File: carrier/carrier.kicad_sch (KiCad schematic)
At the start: 0 parts

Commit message: getting there!!
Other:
- sheet Battery ports: added none; removed +3.3v
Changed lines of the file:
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@@
-    (stroke (width 0) (type solid) (color 0 0 0 0))
-  )
-  (wire (pts (xy 102.235 142.875) (xy 107.95 142.875))
     (stroke (width 0) (type solid) (color 0 0 0 0))
   )
@@
     (effects (font (size 1.27 1.27)) (justify left bottom))
   )
-  (label "+3.3v" (at 102.235 142.875 0)
-    (effects (font (size 1.27 1.27)) (justify left bottom))
-  )
   (label "+1.8v" (at 159.385 50.8 180)
     (effects (font (size 1.27 1.27)) (justify right bottom))
@@
     (pin "BATT" bidirectional (at 146.05 116.205 0)
       (effects (font (size 1.27 1.27)) (justify right))
-    )
-    (pin "+3.3v" input (at 107.95 142.875 180)
-      (effects (font (size 1.27 1.27)) (justify left))
     )
   )
@@
       (reference "#PWR032") (unit 1) (value "GND") (footprint "")
     )
-    (path "/8d0ae364-2b30-4b7c-813a-81b59cbe3cd0/04d39b6f-bef8-4e10-b64f-61ce5ff85de0"
-      (reference "#PWR033") (unit 1) (value "GND") (footprint "")
-    )
     (path "/8d0ae364-2b30-4b7c-813a-81b59cbe3cd0/129c8999-6ac8-415a-99f5-4b344c68b146"
       (reference "#PWR034") (unit 1) (value "GND") (footprint "")
@@
       (reference "#PWR0108") (unit 1) (value "GND") (footprint "")
     )
+    (path "/8d0ae364-2b30-4b7c-813a-81b59cbe3cd0/efacc3e3-b342-4b3e-90b1-8a3c97601e01"
+      (reference "#PWR0109") (unit 1) (value "GNDA") (footprint "")
+    )
     (path "/59fee1d9-7f44-408e-bd4e-36f39b8a6086/c8a711c2-5c9c-43c5-8861-afaf43eb0347"

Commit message: Auto stash before merge of "master" and "origin/master"
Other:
- removed sheet Battery

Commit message: a
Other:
- sheet Buttons ports: added 3v3; removed +3.3v

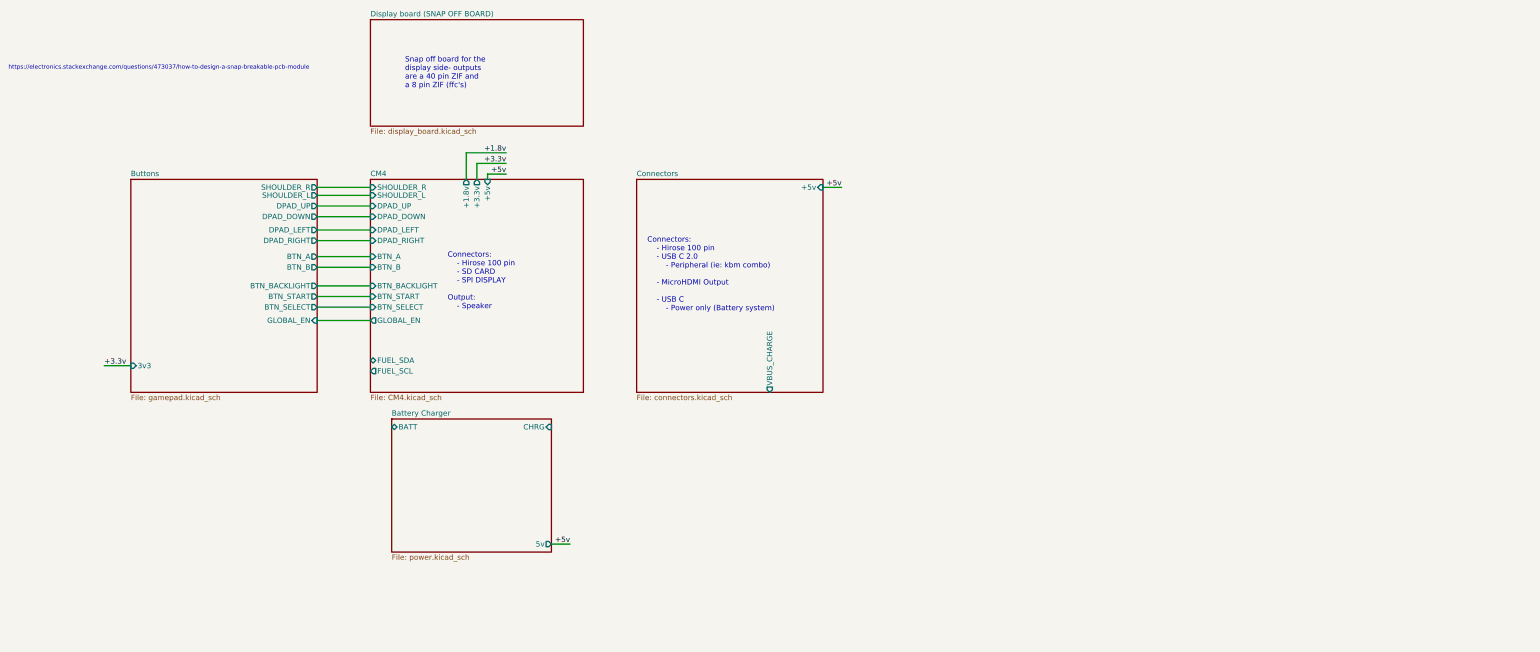
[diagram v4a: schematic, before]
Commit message: add correct charge chip
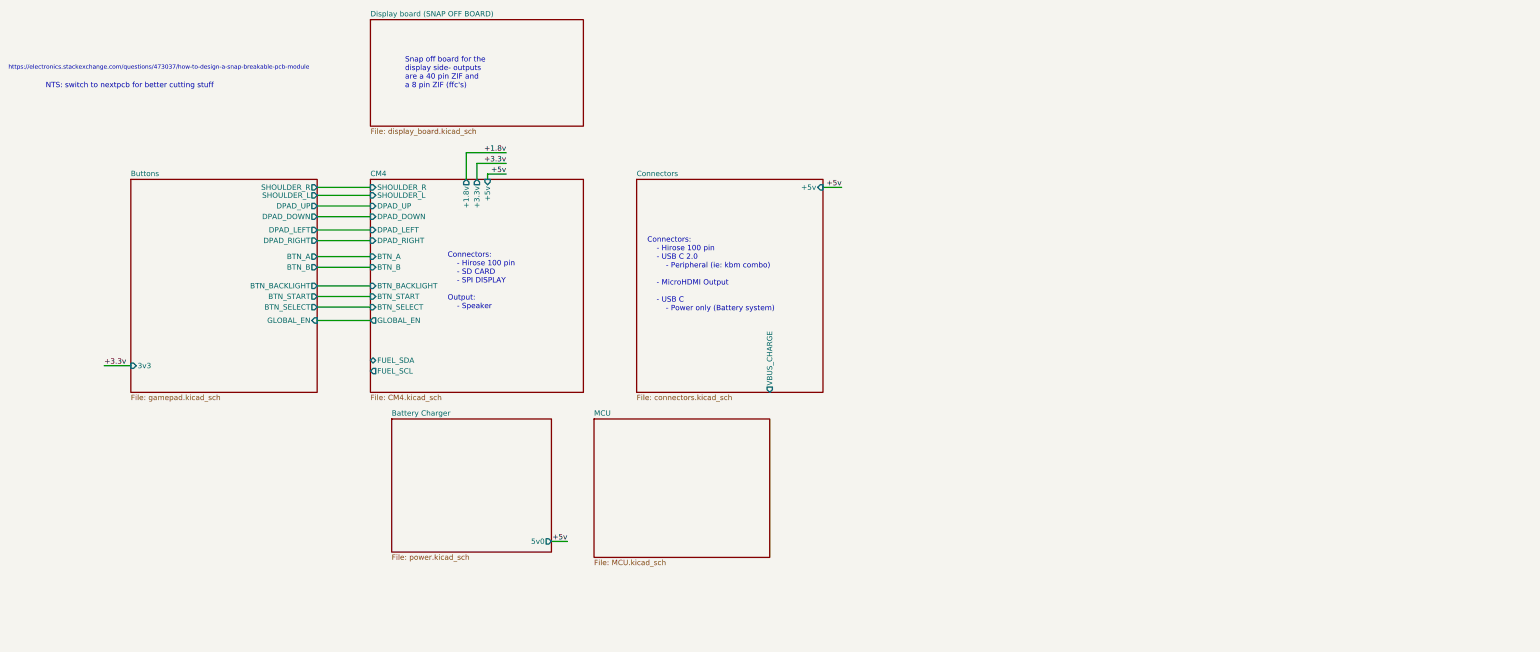
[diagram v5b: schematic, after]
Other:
- added sheet MCU (MCU.kicad_sch)
- sheet Battery Charger ports: added 5v0; removed 5v, BATT, CHRG
- note added: "NTS: switch to nextpcb for better cutting stuff"
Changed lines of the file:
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@@
     (stroke (width 0) (type solid) (color 0 0 0 0))
   )
-  (wire (pts (xy 170.18 144.145) (xy 174.625 144.145))
+  (wire (pts (xy 170.18 143.51) (xy 173.99 143.51))
     (stroke (width 0) (type solid) (color 0 0 0 0))
   )
@@
     (effects (font (size 1.016 1.016)) (justify left bottom))
   )
+  (text "NTS: switch to nextpcb for better cutting stuff\n" (at 49.53 35.56 0)
+    (effects (font (size 1.27 1.27)) (justify left bottom))
+  )
   (text "Snap off board for the\ndisplay side- outputs \nare a 40 pin ZIF and \na 8 pin ZIF (ffc's)"
     (at 135.255 35.56 0)
@@
     (effects (font (size 1.27 1.27)) (justify right bottom))
   )
-  (label "+5v" (at 174.625 144.145 180)
+  (label "+5v" (at 173.99 143.51 180)
     (effects (font (size 1.27 1.27)) (justify right bottom))
   )
@@
       (effects (font (size 1.27 1.27)) (justify left top))
     )
-    (pin "5v" output (at 170.18 144.145 0)
-      (effects (font (size 1.27 1.27)) (justify right))
-    )
-    (pin "CHRG" input (at 170.18 116.205 0)
-      (effects (font (size 1.27 1.27)) (justify right))
-    )
-    (pin "BATT" bidirectional (at 132.08 116.205 180)
-      (effects (font (size 1.27 1.27)) (justify left))
+    (pin "5v0" output (at 170.18 143.51 0)
+      (effects (font (size 1.27 1.27)) (justify right))
     )
   )
@@
     )
     (property "Sheet file" "display_board.kicad_sch" (id 1) (at 127 44.9587 0)
+      (effects (font (size 1.27 1.27)) (justify left top))
+    )
+  )
+  (sheet (at 180.34 114.3) (size 41.91 33.02) (fields_autoplaced)
+    (stroke (width 0.0006) (type solid) (color 0 0 0 0))
+    (fill (color 0 0 0 0.0000))
+    (property "Sheet name" "MCU" (id 0) (at 180.34 113.6643 0)
+      (effects (font (size 1.27 1.27)) (justify left bottom))
+    )
+    (property "Sheet file" "MCU.kicad_sch" (id 1) (at 180.34 147.8287 0)
       (effects (font (size 1.27 1.27)) (justify left top))
     )
@@
     (path "/7d2c72bb-6811-42b4-a3fa-d7ba2c227aca" (page "5"))
     (path "/95ef1699-d890-4da8-941a-b0ab341c2e25" (page "6"))
+    (path "/77193d89-78c6-4010-825b-a155aec2e93e" (page "7"))
   )
   (symbol_instances
@@
       (reference "#PWR0106") (unit 1) (value "GND") (footprint "")
     )
+    (path "/8d0ae364-2b30-4b7c-813a-81b59cbe3cd0/166e9dc6-af9b-47eb-84da-ee8bc34e7cba"
+      (reference "#PWR?") (unit 1) (value "GND") (footprint "")
+    )
     (path "/59fee1d9-7f44-408e-bd4e-36f39b8a6086/4d9af2ac-c03b-4a4e-8907-e039a495780e"
       (reference "#PWR?") (unit 1) (value "GND") (footprint "")
@@
       (reference "#PWR?") (unit 1) (value "GND") (footprint "")
     )
+    (path "/8d0ae364-2b30-4b7c-813a-81b59cbe3cd0/6783b27c-2fe6-4a5d-bb03-3af7211d20d6"
+      (reference "#PWR?") (unit 1) (value "GND") (footprint "")
+    )
     (path "/59fee1d9-7f44-408e-bd4e-36f39b8a6086/878f59a1-d98a-44b7-b33d-cb5bbbc68873"
       (reference "#PWR?") (unit 1) (value "GND") (footprint "")
@@
     )
     (path "/59fee1d9-7f44-408e-bd4e-36f39b8a6086/e68faf50-b903-4194-b057-4ae0ffc47bdc"
+      (reference "#PWR?") (unit 1) (value "GND") (footprint "")
+    )
+    (path "/8d0ae364-2b30-4b7c-813a-81b59cbe3cd0/e78a45a7-0f1c-44a9-9971-70b231727540"
+      (reference "#PWR?") (unit 1) (value "GND") (footprint "")
+    )
+    (path "/8d0ae364-2b30-4b7c-813a-81b59cbe3cd0/f27f7bc6-ead5-427c-9279-8a83b87b910d"
       (reference "#PWR?") (unit 1) (value "GND") (footprint "")
     )
@@
       (reference "C?") (unit 1) (value "100n") (footprint "")
     )
+    (path "/8d0ae364-2b30-4b7c-813a-81b59cbe3cd0/0e79096d-0c34-44d1-8b61-c959a6fcb9e5"
+      (reference "C?") (unit 1) (value "C") (footprint "")
+    )
     (path "/59fee1d9-7f44-408e-bd4e-36f39b8a6086/12eda176-abcb-410e-8d83-2ae9138fed10"
       (reference "C?") (unit 1) (value "100n") (footprint "")
     )
+    (path "/8d0ae364-2b30-4b7c-813a-81b59cbe3cd0/15397f92-ae9f-4d5e-8e60-683e8d1f87c6"
+      (reference "C?") (unit 1) (value "C") (footprint "")
+    )
     (path "/59fee1d9-7f44-408e-bd4e-36f39b8a6086/15a435a9-04c2-4f0e-a02c-d692f26f1cb9"
       (reference "C?") (unit 1) (value "100n") (footprint "")
@@
       (reference "C?") (unit 1) (value "100n") (footprint "")
     )
+    (path "/8d0ae364-2b30-4b7c-813a-81b59cbe3cd0/1beeac18-d598-4261-ac46-ffdc983c432a"
+      (reference "C?") (unit 1) (value "C") (footprint "")
+    )
     (path "/8d0ae364-2b30-4b7c-813a-81b59cbe3cd0/1e02c2ec-7180-4051-bae7-ee592aae0f7c"
       (reference "C?") (unit 1) (value "C") (footprint "")
@@
       (reference "C?") (unit 1) (value "100n") (footprint "")
     )
+    (path "/8d0ae364-2b30-4b7c-813a-81b59cbe3cd0/431bd8b9-631e-41b0-9143-1b1273ae68f1"
+      (reference "C?") (unit 1) (value "C") (footprint "")
+    )
+    (path "/8d0ae364-2b30-4b7c-813a-81b59cbe3cd0/4edc541e-b62c-49b9-b29f-3071842e7229"
+      (reference "C?") (unit 1) (value "C") (footprint "")
+    )
     (path "/8d0ae364-2b30-4b7c-813a-81b59cbe3cd0/6d717528-6e17-405b-8556-4a14a8a13069"
       (reference "C?") (unit 1) (value "C") (footprint "")
     )
+    (path "/8d0ae364-2b30-4b7c-813a-81b59cbe3cd0/751a09af-9429-4bdc-9a06-5d2d06fbad8e"
+      (reference "C?") (unit 1) (value "C") (footprint "")
+    )
     (path "/59fee1d9-7f44-408e-bd4e-36f39b8a6086/889b2d74-d9a9-447a-a177-6dd84c72334a"
       (reference "C?") (unit 1) (value "100n") (footprint "")
@@
       (reference "C?") (unit 1) (value "100n") (footprint "")
     )
+    (path "/8d0ae364-2b30-4b7c-813a-81b59cbe3cd0/b1a1e955-947f-4789-8cb5-7e8a9d28d9d2"
+      (reference "C?") (unit 1) (value "C") (footprint "")
+    )
     (path "/8d0ae364-2b30-4b7c-813a-81b59cbe3cd0/cb449799-0847-4526-b674-c4a0845ba779"
       (reference "C?") (unit 1) (value "C") (footprint "")
     )
     (path "/8d0ae364-2b30-4b7c-813a-81b59cbe3cd0/cd680b00-cb5e-4454-88f6-b5aa1013a0f3"
+      (reference "C?") (unit 1) (value "C") (footprint "")
+    )
+    (path "/8d0ae364-2b30-4b7c-813a-81b59cbe3cd0/cd989e33-ea98-42d8-904e-682def6197ce"
       (reference "C?") (unit 1) (value "C") (footprint "")
     )
@@
       (reference "J7") (unit 1) (value "AudioJack3_Switch") (footprint "audio:audio")
     )
+    (path "/8d0ae364-2b30-4b7c-813a-81b59cbe3cd0/29dfa63d-920a-41d7-8f66-f494c720f779"
+      (reference "L?") (unit 1) (value "L") (footprint "")
+    )
     (path "/8d0ae364-2b30-4b7c-813a-81b59cbe3cd0/89babfe2-3c32-49eb-9968-55ade52617ed"
       (reference "L?") (unit 1) (value "L") (footprint "")
@@
       (reference "U4") (unit 1) (value "AP22814AW5") (footprint "Package_TO_SOT_SMD:SOT-23-5")
     )
+    (path "/8d0ae364-2b30-4b7c-813a-81b59cbe3cd0/4b6a6b94-9308-4d46-897f-e144e98a83a9"
+      (reference "U?") (unit 1) (value "LM8850") (footprint "")
+    )
     (path "/8d0ae364-2b30-4b7c-813a-81b59cbe3cd0/7206af90-fe4a-4499-b72a-f7b8a2d50387"

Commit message: thingy
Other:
- added sheet Untitled Sheet (untitled.kicad_sch)
- sheet Battery Charger ports: added BTN_POWER; removed none
- sheet Buttons ports: added 5v; removed none
- sheet CM4 ports: added TXD_POW; removed none
- sheet MCU ports: added BTN_POW; removed none
- note added: "When TXD_POW is low state - no effect When TXD_POW is high state -"
